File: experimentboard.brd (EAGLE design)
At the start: 152.4 x 100 mm, 171 parts, among them IC1 TL072P, IC2 LM317, IC3 LM337, IC4 TL072P, IC5 TL072P, IC6 TL072P, U1 PCM1690, U2 DIR9001, U3 CAT24C256

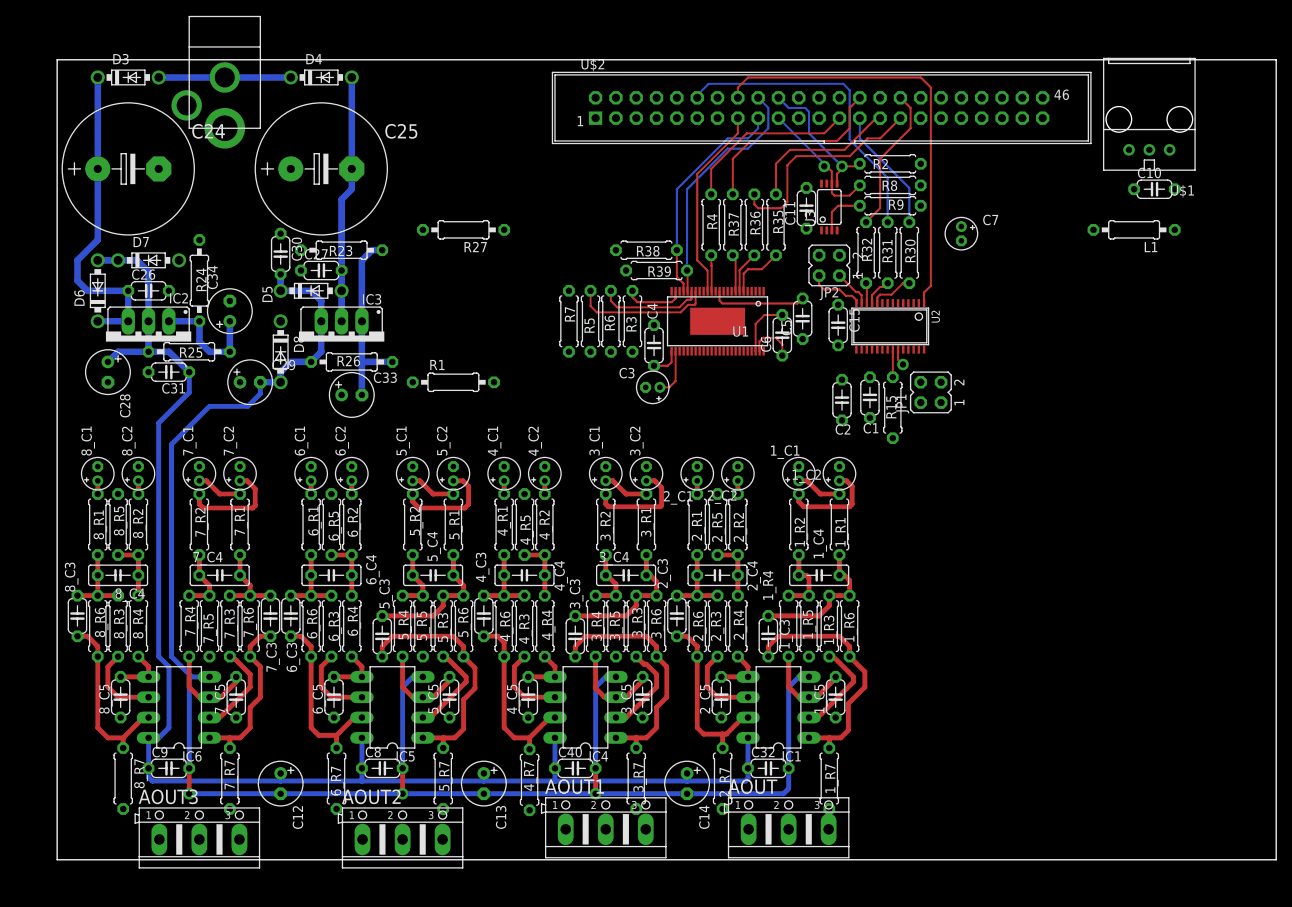
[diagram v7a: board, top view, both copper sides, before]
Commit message: Rotated PSU section, and more work since
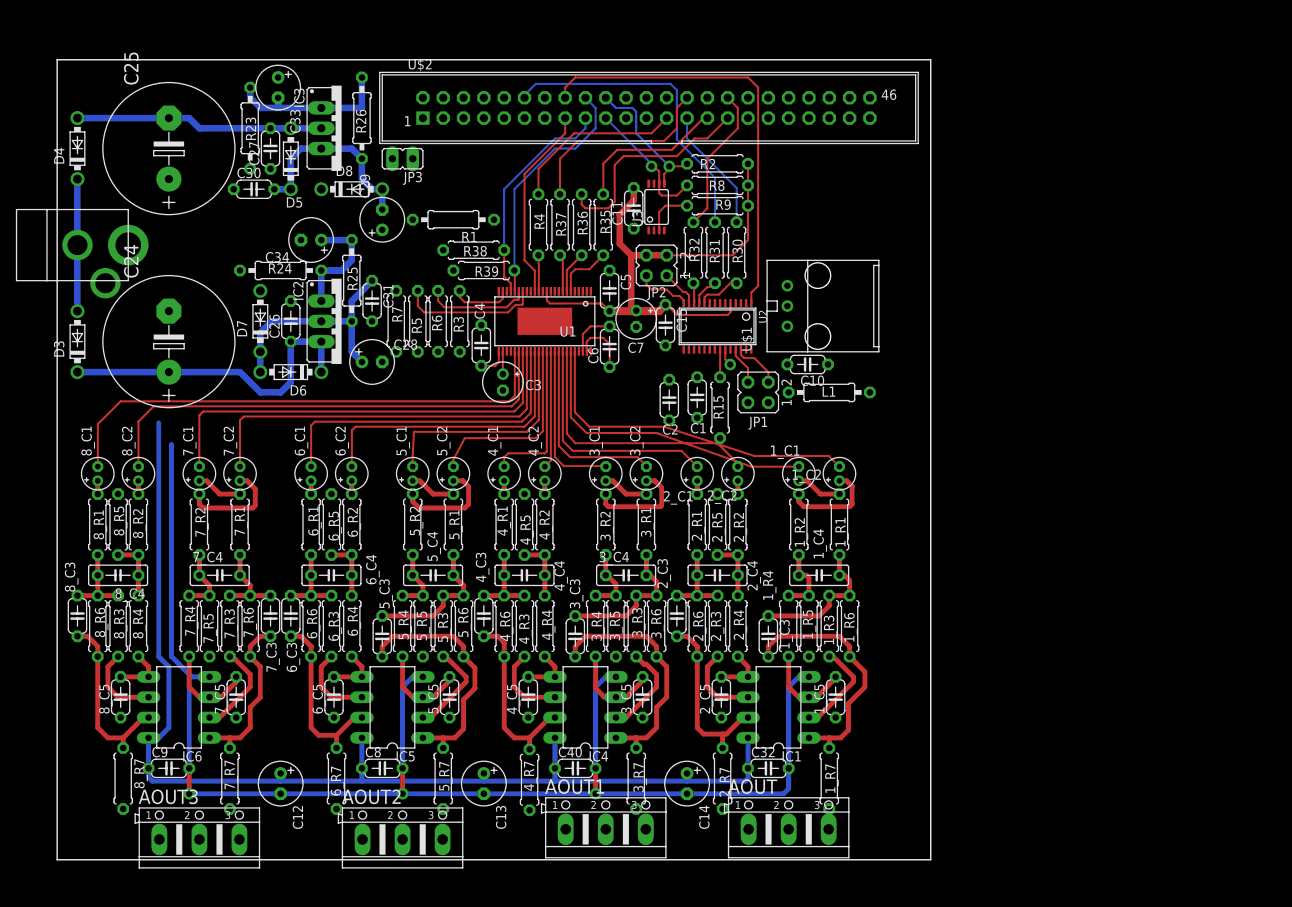
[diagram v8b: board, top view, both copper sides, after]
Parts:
- removed R27: 0, rcl:0207/10
- added JP3: (no value), jumper:JP1
- C3: device rcl:E1,8-4 -> rcl:E2-5
- C7: value 10 µF -> 22uF; device rcl:E1,8-4 -> rcl:E2-5
- moved U$1 53.9 mm to (102.7, 63.5), turned to 90 degrees
- moved C10 48.6 mm to (93.8, 61.9), turned to 180 degrees
- moved L1 43.2 mm to (96.5, 58.4), turned to 0 degrees
- moved C7 42.0 mm to (72.4, 67.6)
- moved C33 39.5 mm to (27.6, 96.5), turned to 270 degrees
- moved AC 39.5 mm to (-5.08, 72.4), turned to 90 degrees
- moved D3 33.6 mm to (2.54, 64.8), turned to 90 degrees
- moved C28 33.0 mm to (39.4, 62.2), turned to 0 degrees
- moved D4 31.8 mm to (2.54, 88.9), turned to 90 degrees
- moved R26 30.5 mm to (38.1, 92.7), turned to 90 degrees
- moved C31 26.9 mm to (39.4, 69.8), turned to 270 degrees
- moved IC3 26.7 mm to (35.6, 91.4), turned to 270 degrees
- moved C29 26.2 mm to (40.6, 80.0), turned to 90 degrees
- moved D6 26.2 mm to (29.2, 61.0), turned to 180 degrees
- moved C5 24.4 mm to (69.1, 71.1), turned to 270 degrees
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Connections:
- net N$12 renamed VCOM
- net V+: now also JP3.2; no longer R27.2
- net VCC: now also JP3.1; no longer R27.1
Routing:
- net VOUT8+: track 0.00 -> 64.5 mm
- net VOUT8-: track 0.00 -> 60.3 mm
- net VDD: track 12.0 -> 68.3 mm
- net VOUT7+: track 0.00 -> 53.9 mm
- net VOUT7-: track 0.00 -> 49.4 mm
- net VOUT1-: track 0.00 -> 42.6 mm
- net VOUT6+: track 0.00 -> 40.9 mm
- net VOUT1+: track 0.00 -> 38.3 mm
- net VOUT6-: track 0.00 -> 36.3 mm
- net VOUT2-: track 0.00 -> 33.6 mm
- net VOUT2+: track 0.00 -> 29.3 mm
- net VOUT5+: track 0.00 -> 29.2 mm
- net VOUT5-: track 0.00 -> 24.0 mm
- net VOUT3-: track 0.00 -> 23.9 mm
- net VOUT3+: track 0.00 -> 20.1 mm
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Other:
- board size 152.4 x 100 mm -> 109.2 x 100 mm
